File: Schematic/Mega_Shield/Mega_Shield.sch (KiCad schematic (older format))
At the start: 29 parts, among them J1 Mini-DIN-4, J10 Conn_01x08, J11 Conn_01x08, J12 Conn_02x18_Odd_Even, J13 Conn_01x08, J14 Conn_01x08, J15 Conn_01x08, J16 Conn_01x10, J2 Mini-DIN-4, J3 Mini-DIN-4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

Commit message: Upadeted PCB design for Logger and for TTS
Mega updated for BLE and reduced in size. Nano shield updated for
MLX90621 array based sensor
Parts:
- removed C?: 2.2uF, Capacitor_THT:C_Rect_L4.0mm_W2.5mm_P2.50mm, symbol Device:C
- removed C? (x2): 0.1uF, Capacitor_THT:C_Rect_L4.0mm_W2.5mm_P2.50mm, symbol Device:C
- removed C?: 10nF, Capacitor_THT:C_Rect_L4.0mm_W2.5mm_P2.50mm, symbol Device:C
- removed J10, J11, J13, J14, J15: Conn_01x08, Connector_PinSocket_2.54mm:PinSocket_1x08_P2.54mm_Vertical, symbol Connector_Generic:Conn_01x08
- removed J12: Conn_02x18_Odd_Even, TTS-UART:PinSocket_2x18_P2.54mm_Vertical_Swapped, symbol Connector_Generic:Conn_02x18_Odd_Even
- removed J16: Conn_01x10, Connector_PinSocket_2.54mm:PinSocket_1x10_P2.54mm_Vertical, symbol Connector_Generic:Conn_01x10
- removed J2: Mini-DIN-4, TTS-UART:KMDGX-4S-BS, symbol Connector:Mini-DIN-4
- removed J5: Screw_Terminal_01x02, TerminalBlock_Phoenix:TerminalBlock_Phoenix_PT-1,5-2-5.0-H_1x02_P5.00mm_Horizontal, symbol Connector:Screw_Terminal_01x02
- removed J6: SF_OBDII, Connector_PinHeader_2.54mm:PinHeader_1x03_P2.54mm_Vertical, symbol Connector:Conn_01x03_Male
- removed U?: ICM-20602, Package_LGA:LGA-16_3x3mm_P0.5mm_LayoutBorder3x5y, symbol Sensor_Motion:ICM-20602
- added J2: Conn_01x04_Female, Onboard_Sensors:Voltage_Regulator, symbol Connector:Conn_01x04_Female
- added J6: BLE HC-05, Onboard_Sensors:BLEHC-05, symbol Connector:Conn_01x06_Male
- added J7: MPU 6050, Onboard_Sensors:GY-521, symbol Connector:Conn_01x08_Male
- D1, D2: footprint Diode_SMD:D_SOD-923 -> Diode_THT:D_DO-41_SOD81_P10.16mm_Horizontal
- D3: footprint TTS-UART:KBP306GTB -> TTS-URAT:KBP306GTB
- D4: footprint digikey-kicad-library:LED_3mm_Radial -> Digikey:LED_3mm_Radial
- J1, J3, J4: footprint TTS-UART:KMDGX-4S-BS -> TTS-URAT:RHT-634-1261-1
- J9: footprint Onboard_Sensors:SD_Module -> Onboard_Sensors:SD_Module_Vertical
- U1: footprint TTS-UART:ISL81487EIPZ-PDIP -> TTS-URAT:ISL81487EIPZ-PDIP; symbol TTS_UART:ISL81487EIPZ -> Mega_Shield-rescue:ISL81487EIPZ-TTS_UART
- XA1: symbol arduino:Arduino_Mega2560_Shield -> Mega_Shield-rescue:Arduino_Mega2560_Shield-arduino
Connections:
- net 5V is gone; now on net VCC: XA1.5V1 (5V), XA1.5V3 (5V), XA1.5V4 (5V)
- net A4: now also J7.5 (Pin_5)
- net A5: now also J7.6 (Pin_6)
- net D16: now also J6.2 (Pin_2)
- net D17: now also J6.3 (Pin_3)
- net D2: now also J7.3 (Pin_3)
- net GND: now also D4.1 (K), J1.1, J4.1, J2.3 (Pin_3), J6.4 (Pin_4), J7.4 (Pin_4), J7.7 (Pin_7)
- net VCC: now also J6.5 (Pin_5), J7.8 (Pin_8); no longer D4.1 (K)
- net VIN: now also J1.2, J4.2, J2.4 (Pin_4); no longer D3.1 (+)
- net at D2.1 (K), J1.3, J4.3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: no longer J3.3
- net at D1.1 (K), J1.4, J4.4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: no longer J3.4
- new net: D3.1 (+), J2.2 (Pin_2)
- new net: D3.2 (~~), J3.1
- new net: D3.3 (~~), J3.2
- no-connect marks 7 -> 11
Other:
- moved on the sheet: D2, D3

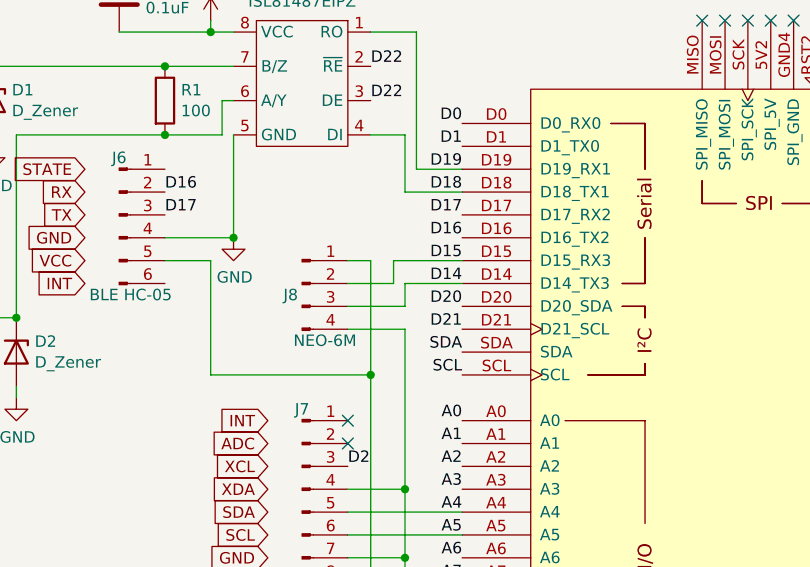
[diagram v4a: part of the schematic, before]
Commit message: Udated logger and TTS for full sensor suit
2.2 Basic Sensor Suit and 2.6 Array Based Tire Temps
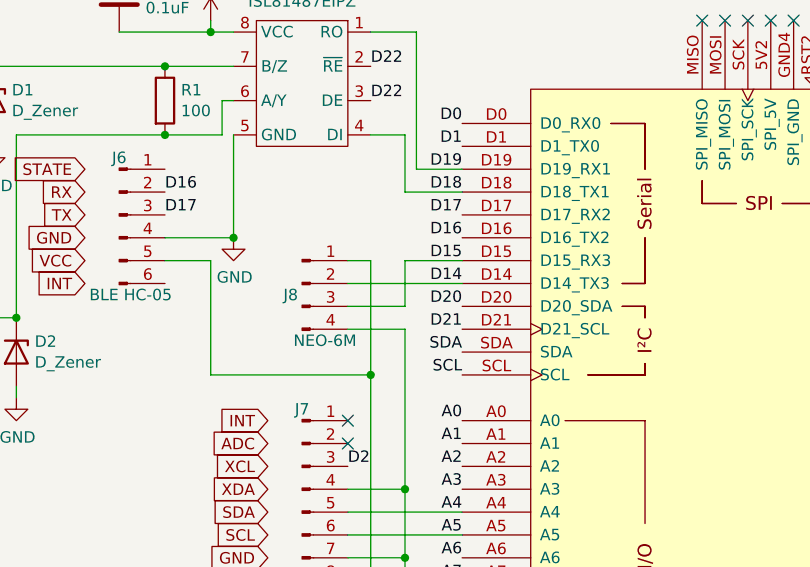
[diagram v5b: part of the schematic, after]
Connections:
- net D14: now also J8.2 (Pin_2); no longer J8.3 (Pin_3)
- net D15: now also J8.3 (Pin_3); no longer J8.2 (Pin_2)
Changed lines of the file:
@@
 Wire Wire Line
 	3850 2350 4100 2350
-Wire Wire Line
-	4100 2250 4350 2250
-Wire Wire Line
-	4100 2350 4100 2250
-Wire Wire Line
-	3850 2250 4050 2250
-Wire Wire Line
-	4050 2150 4350 2150
-Wire Wire Line
-	4050 2250 4050 2150
 $Comp
 L power:VDD #PWR019
@@
 NoConn ~ 2650 7100
 NoConn ~ 2050 7100
+Wire Wire Line
+	3850 2250 4350 2250
+Wire Wire Line
+	4100 2350 4100 2150
+Wire Wire Line
+	4100 2150 4350 2150
 $EndSCHEMATC

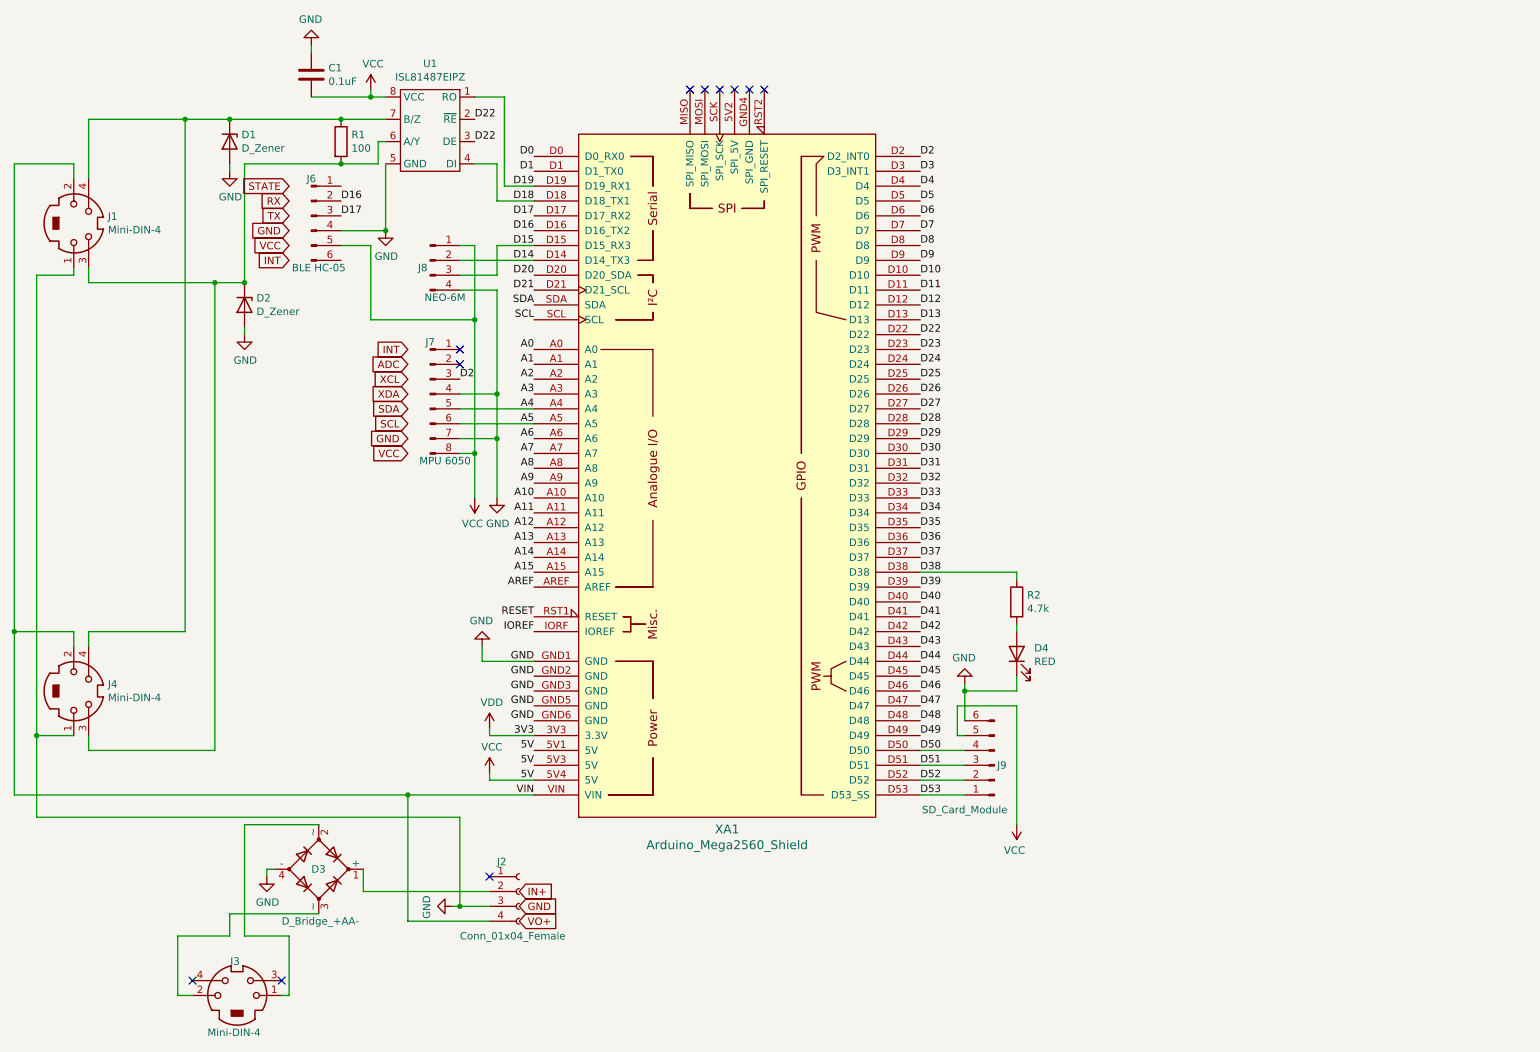
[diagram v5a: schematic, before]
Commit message: Verion 4 PCB and Code
Updated PCB layout for version 4; for both TTS and Logger.
Updated code to asign ID to TTS and to send data via BT
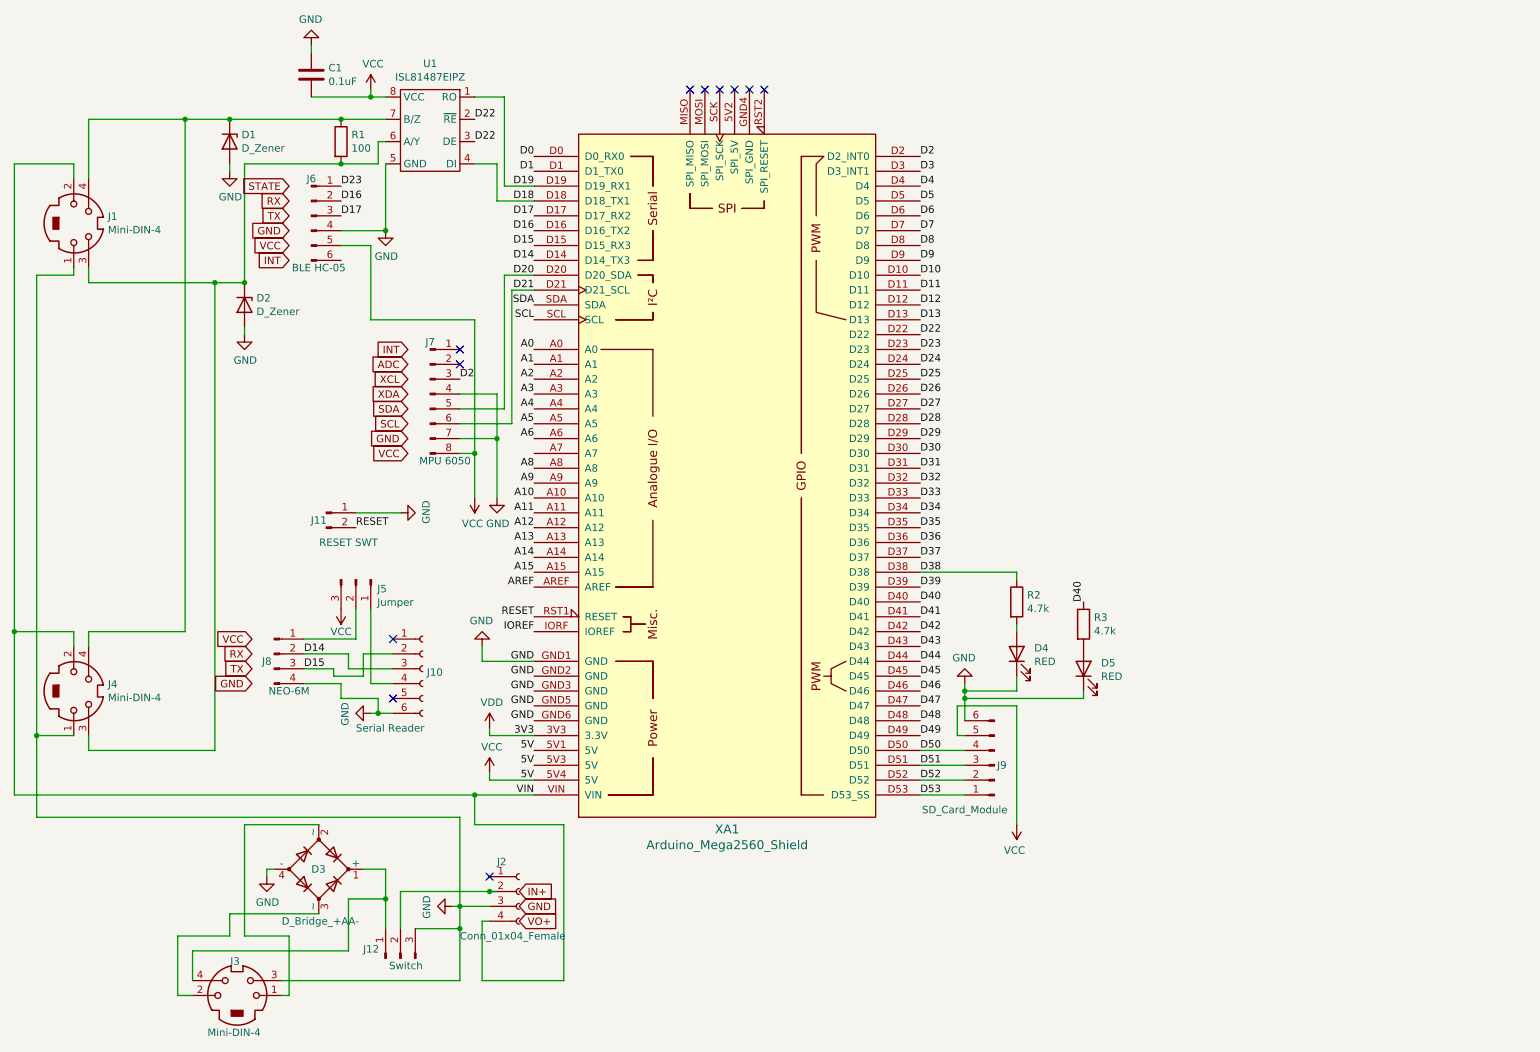
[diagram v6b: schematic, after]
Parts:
- added D5: RED, Digikey:LED_3mm_Radial, symbol Device:LED
- added J10: Serial Reader, Connector_PinSocket_2.54mm:PinSocket_1x06_P2.54mm_Vertical, symbol Connector:Conn_01x06_Female
- added J11: RESET SWT, Connector_PinSocket_2.54mm:PinSocket_1x02_P2.54mm_Vertical, symbol Connector:Conn_01x02_Male
- added J12: Switch, Connector_PinSocket_2.54mm:PinSocket_1x03_P2.54mm_Vertical, symbol Connector:Conn_01x03_Male
- added J5: Jumper, Connector_PinSocket_2.54mm:PinSocket_1x03_P2.54mm_Vertical, symbol Connector:Conn_01x03_Male
- added R3: 4.7k, Resistor_THT:R_Axial_DIN0204_L3.6mm_D1.6mm_P5.08mm_Horizontal, symbol Device:R
- J1, J3, J4: footprint TTS-URAT:RHT-634-1261-1 -> Connector_PinSocket_2.54mm:PinSocket_2x02_P2.54mm_Vertical
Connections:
- net A4: no longer J7.5 (Pin_5)
- net A5: no longer J7.6 (Pin_6)
- net D14: now also J10.3 (Pin_3)
- net D15: now also J10.2 (Pin_2)
- net D20: now also J7.5 (Pin_5)
- net D21: now also J7.6 (Pin_6)
- net D23: now also J6.1 (Pin_1)
- net D40: now also R3.1
- net GND: now also J3.3, D5.1 (K), J10.6 (Pin_6), J11.1 (Pin_1), J12.3 (Pin_3)
- net RESET: now also J11.2 (Pin_2)
- net VCC: now also J5.3 (Pin_3); no longer J8.1 (Pin_1)
- net at D3.1 (+): now also J3.4, J12.1 (Pin_1); no longer J2.2 (Pin_2)
- net A7: no longer names the net of XA1.A7
- new net: J5.2 (Pin_2), J8.1 (Pin_1)
- new net: J12.2 (Pin_2), J2.2 (Pin_2)
- new net: J10.4 (Pin_4), J5.1 (Pin_1)
- new net: D5.2 (A), R3.2
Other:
- moved on the sheet: J8
